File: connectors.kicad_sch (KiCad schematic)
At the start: 10 parts, among them J10 SM02B-SRSS-TB(LF)(SN), J11 SM02B-SRSS-TB(LF)(SN), J6 SM04B-SRSS-TB(LF)(SN), J7 SM04B-SRSS-TB(LF)(SN), J8 SM04B-SRSS-TB(LF)(SN), J9 SM04B-SRSS-TB(LF)(SN)

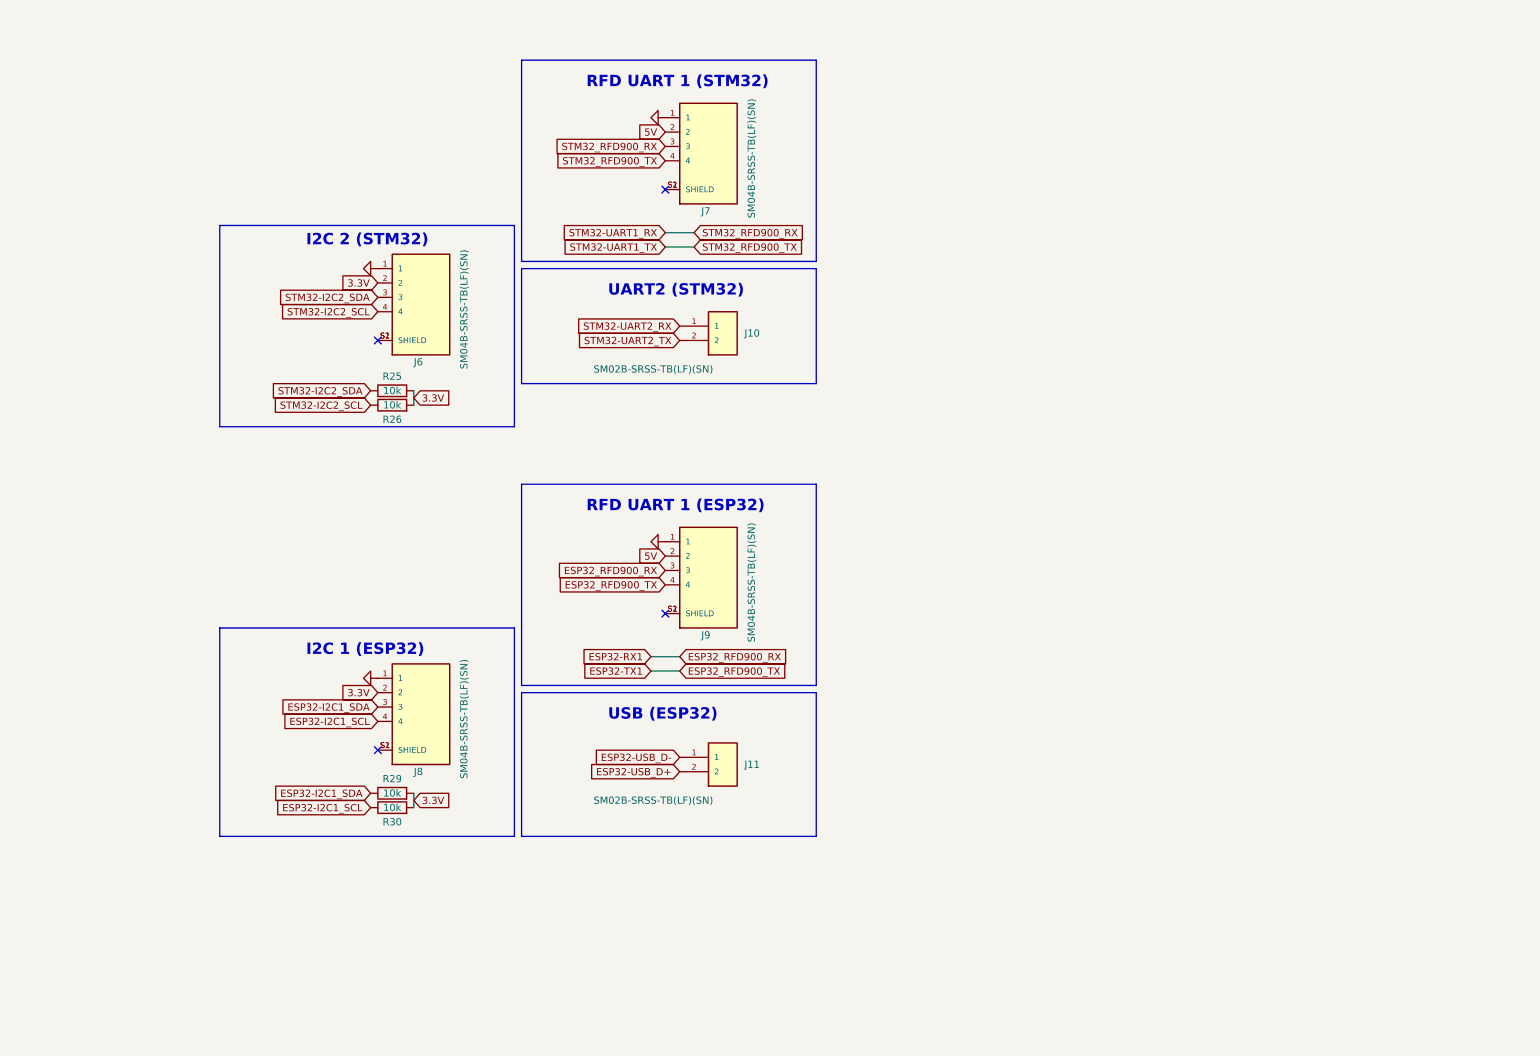
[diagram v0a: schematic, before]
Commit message: Organized Schematics & Fixed Notes
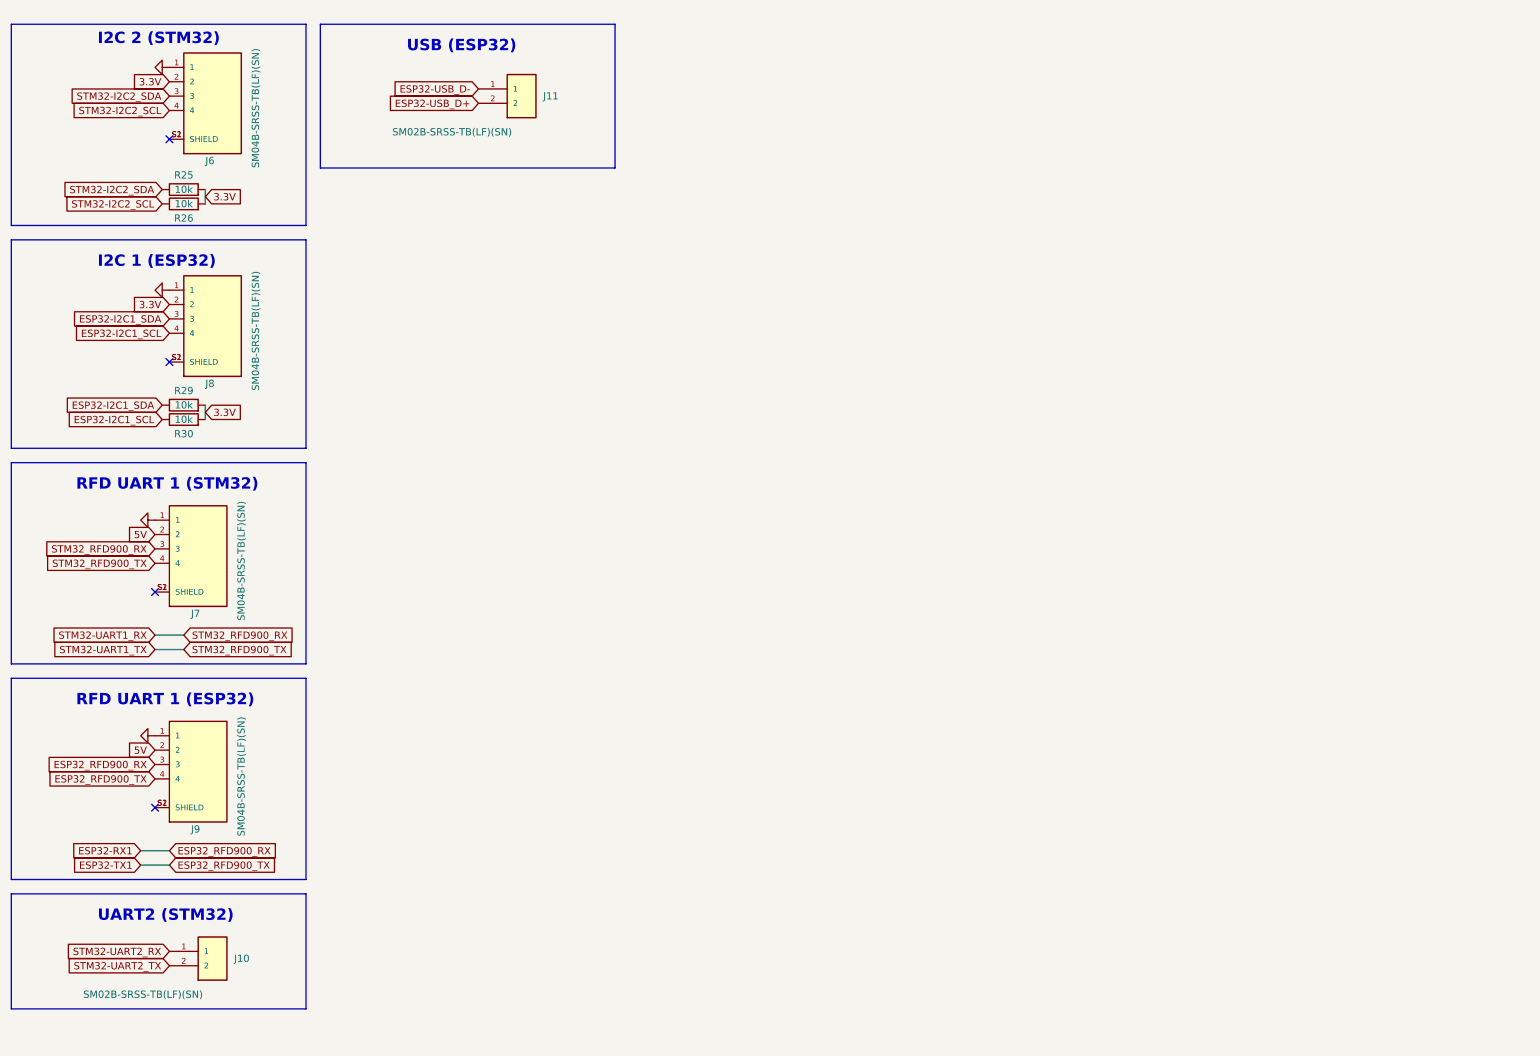
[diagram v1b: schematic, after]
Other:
- company: (none) -> nyuad.space
- title: (none) -> Connectors & Peripherals
- moved on the sheet: J10, J11, J6, J7, J8, J9, R25, R26, R29, R30

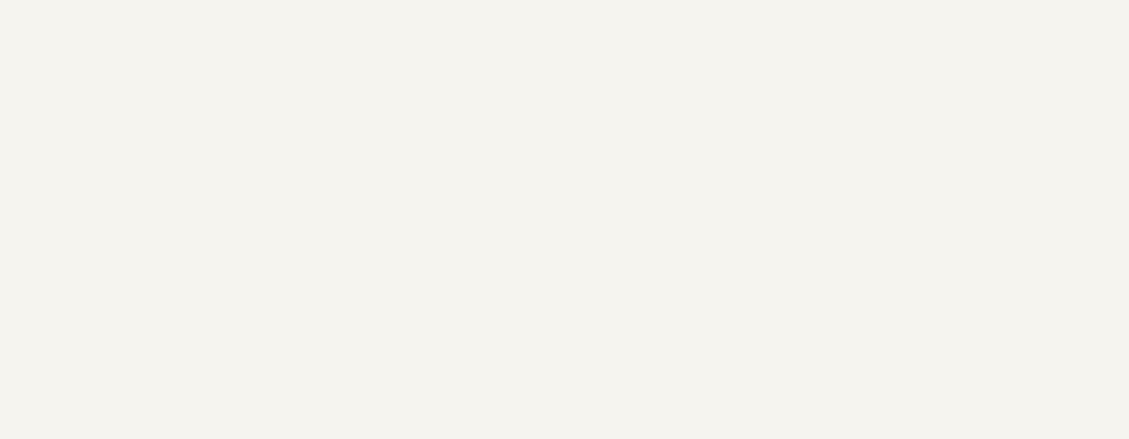
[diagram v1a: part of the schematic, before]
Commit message: Added OSH Logo
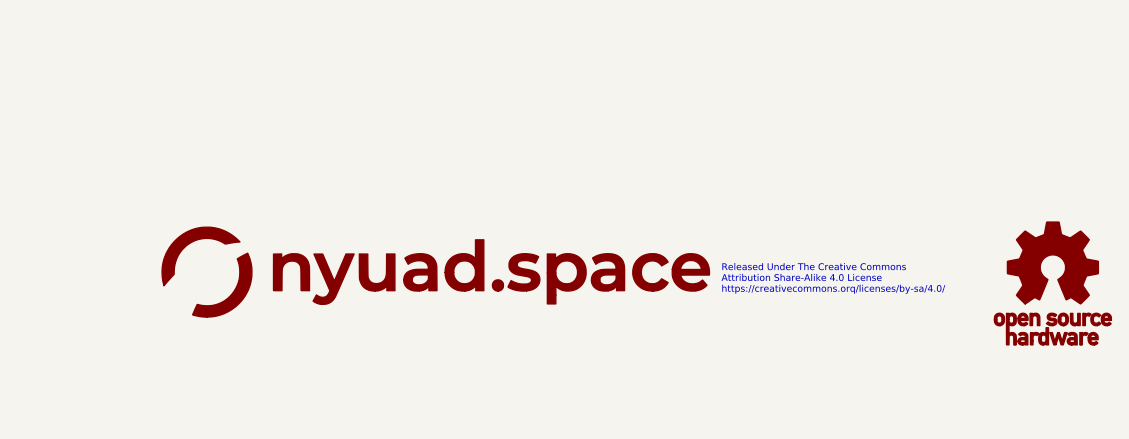
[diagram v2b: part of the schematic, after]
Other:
- note added: "Released Under The Creative Commons Attribution Share-Alike 4.0 License https://creativecommons.orq/licenses/by-sa/4.0/"
- company: nyuad.space -> Aether Flight Computer
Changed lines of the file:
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@@
   (title_block
     (title "Connectors & Peripherals")
-    (company "nyuad.space")
-    (comment 1 "Aether Flight Computer")
+    (company "Aether Flight Computer")
   )
   (no_connect (at 40.64 115.57))
@@
     (effects (font (size 2 2) (thickness 0.8) bold) (justify left bottom))
   )
+  (text "Released Under The Creative Commons\nAttribution Share-Alike 4.0 License\nhttps://creativecommons.orq/licenses/by-sa/4.0/"
+    (at 240.03 175.26 0)
+    (effects (font (face "KiCad Font") (size 0.75 0.75)) (justify left bottom))
+  )
   (text "USB (ESP32)" (at 85.09 20.32 0)
     (effects (font (size 2 2) (thickness 0.8) bold) (justify left bottom))
@@
     )
   )
+  (symbol (lib_id "nyuad_space:LOGO") (at 208.28 172.72 0) (unit 1)
+    (in_bom yes) (on_board yes) (dnp no) (fields_autoplaced)
+    (property "Reference" "#G2" (at 208.28 168.3609 0)
+      (effects (font (size 1.27 1.27)) hide)
+    )
+    (property "Value" "LOGO" (at 208.28 177.0791 0)
+      (effects (font (size 1.27 1.27)) hide)
+    )
+    (property "Footprint" "" (at 208.28 172.72 0)
+      (effects (font (size 1.27 1.27)) hide)
+    )
+    (property "Datasheet" "" (at 208.28 172.72 0)
+      (effects (font (size 1.27 1.27)) hide)
+    )
+    (instances
+      (project "aether"
+        (path "/e12346fa-509d-4de9-8ab1-dced307292db"
+          (reference "#G2") (unit 1)
+        )
+        (path "/e12346fa-509d-4de9-8ab1-dced307292db/7d58c90a-6730-4b63-ae17-c9d1fe4b2f54"
+          (reference "#G7") (unit 1)
+        )
+      )
+    )
+  )
   (symbol (lib_id "SM04B-SRSS-TB_LF__SN_:SM04B-SRSS-TB(LF)(SN)") (at 50.8 67.31 0) (unit 1)
     (in_bom yes) (on_board yes) (dnp no)
@@
         )
       )
+    )
+  )
+  (symbol (lib_id "osh_logo:LOGO") (at 276.86 173.99 0) (unit 1)
+    (in_bom yes) (on_board yes) (dnp no) (fields_autoplaced)
+    (property "Reference" "#G1" (at 276.86 167.7874 0)
+      (effects (font (size 1.27 1.27)) hide)
+    )
+    (property "Value" "LOGO" (at 276.86 180.1926 0)
+      (effects (font (size 1.27 1.27)) hide)
+    )
+    (property "Footprint" "" (at 276.86 173.99 0)
+      (effects (font (size 1.27 1.27)) hide)
+    )
+    (property "Datasheet" "" (at 276.86 173.99 0)
+      (effects (font (size 1.27 1.27)) hide)
+    )
+    (instances
+      (project "aether"
+        (path "/e12346fa-509d-4de9-8ab1-dced307292db"
+          (reference "#G1") (unit 1)
+        )
+        (path "/e12346fa-509d-4de9-8ab1-dced307292db/7d58c90a-6730-4b63-ae17-c9d1fe4b2f54"
+          (reference "#G8") (unit 1)
+        )
+      )

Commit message: Updated files
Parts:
- added J8: SM04B-SRSS-TB(LF)(SN), JST_SM04B-SRSS-TB(LF)(SN), symbol SM04B-SRSS-TB_LF__SN_:SM04B-SRSS-TB(LF)(SN)
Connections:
- new net: J8.S1 (SHIELD), J8.S2 (SHIELD)
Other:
- note added: "0x40, 0x76"
- note added: "0x41"
- note added: "0x42"
- note added: "0x44"
- note added: "I2C 1 (STM32)"
- note added: "SPI 1 (ESP32)"
- note added: "SPI 1 (STM32)"
- note added: "SPI 2 (STM32)"
- note removed: "Released Under The Creative Commons Attribution Share-Alike 4.0 License https://creativecommons.orq/licenses/by-sa/4.0/"
- title: Connectors & Peripherals -> Connections & Peripherals
- moved on the sheet: J11

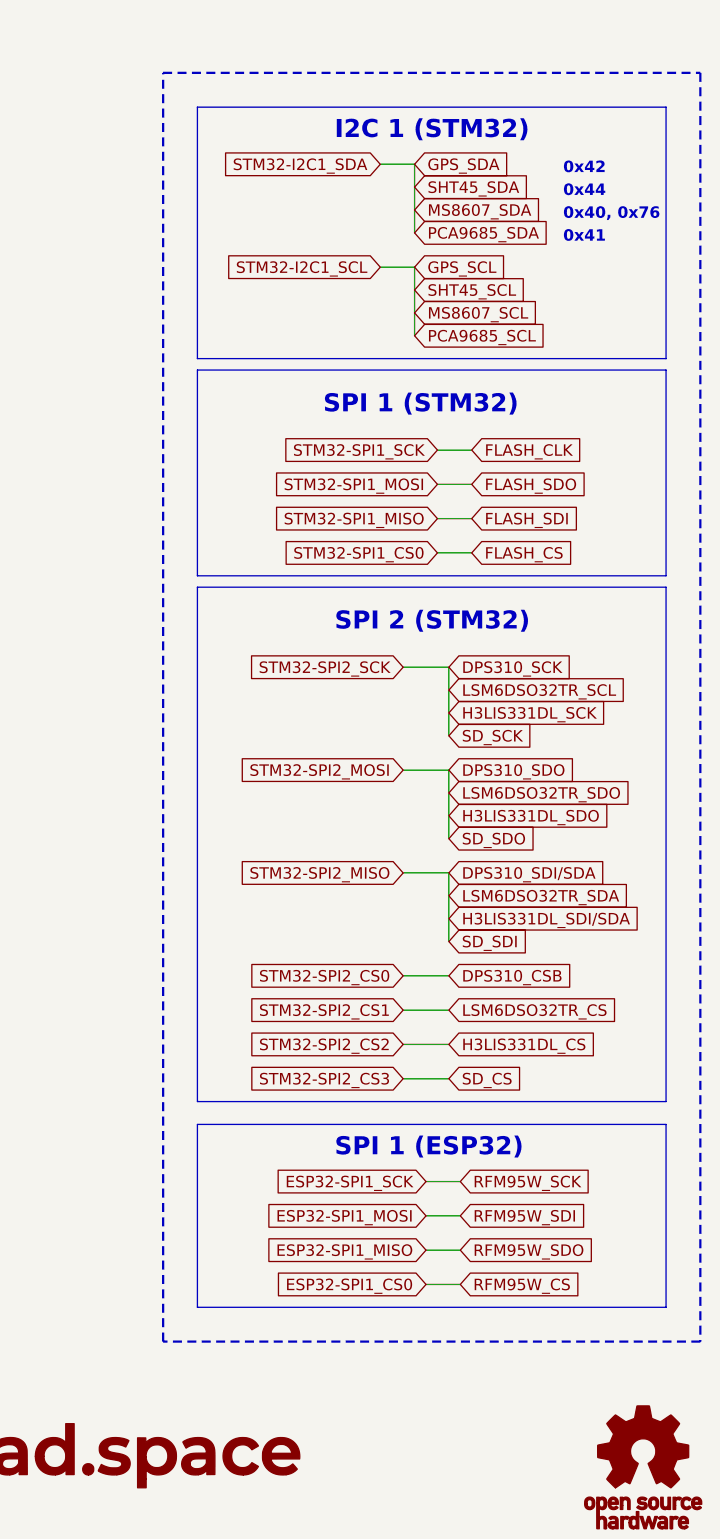
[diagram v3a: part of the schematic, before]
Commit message: Added INA219
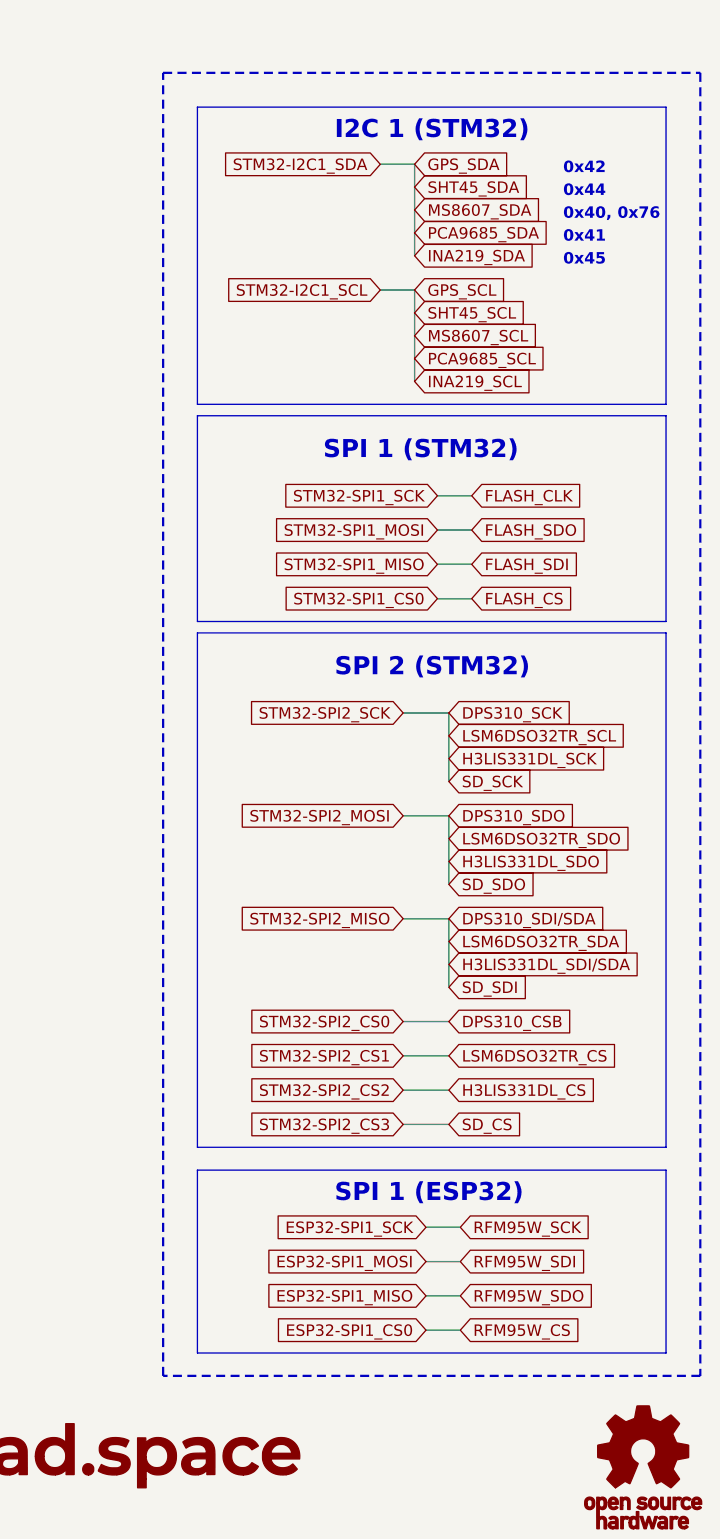
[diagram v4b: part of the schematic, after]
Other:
- note added: "0x45"
